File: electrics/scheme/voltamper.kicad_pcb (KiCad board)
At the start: 2 copper layers, 87 x 64 mm, 147 parts, among them K1 swd, K2 servo-1, K3 servo-2, P1 boot, P10 m3-hole, P11 m3-hole, P12 CONN_13X2, P2 boot, P3 -, P4 +, P5 work, P6 aux, P7 ref, P8 m3-hole, P9 m3-hole, Q1 bc857, Q2 bc847, Q3 bc857, Q4 bc847, Q5 irlml2244, Q6 bc847, Q7 bc847, Q8 bc847, SW1 btn-1, SW2 btn-2, U1 CRYSTAL-4PIN, U10 TDA2030A, U11 INA126, U12 SPARTAN-SIP-9007, U2 CP2102, U3 MICRO-USB-B, U4 MCP1703T-3302E/CB, U5 MCP1703T-3302E/CB, U6 NCP3063, U7 SPARTAN-SIP-9007, U8 NCP3063, U9 SPARTAN-SIP-9007

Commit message: Started placig components.
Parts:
- removed C27, C37, C39, C42: 100n, SM0805
- removed C38: 1u, SM0805
- removed D6: lm258a, SO8E
- removed D8: 1N5819, D3
- added C12: 30n, SM0805, F.Cu at (234.0, 167.0)
- added C18: 1n, SM0805, F.Cu at (218.0, 157.0)
- added R56: 16, SM0805, F.Cu at (221.0, 159.0)
- added R57: 16, SM0805, F.Cu at (223.0, 155.0)
- added R58: 410, SM0805, F.Cu at (214.0, 158.0)
- added R59: 410, SM0805, F.Cu at (219.0, 167.0)
- added R60: 0, SM0805, F.Cu at (219.0, 155.0)
- added R61: 16, SM0805, F.Cu at (223.0, 153.0)
- added R62: 16, SM0805, F.Cu at (213.0, 155.0)
- added R67: 10, R4-5, F.Cu at (232.0, 162.0)
- added R70: 16, SM0805, F.Cu at (225.0, 167.0)
- added R71: 16, SM0805, F.Cu at (230.0, 167.0)
- added U13: OPA551, OPA551, F.Cu at (234.0, 146.0)
- added U14: AD825, SO8E, F.Cu at (210.0, 165.0)
- C20, C26, C35: value 100n -> 4u7
- C23, C25, C30: value 10n -> 4u7
- D4: value lm258a -> 1N5819; footprint SO8E -> D3
- R17: value 10k -> 120k
- R18: value 10k -> 10k 0.1%
- R20: value 10 -> 1k
- R25: value 6k8 -> 13.3k 0.1%
- R26: value 1k -> 120k
- R30: value 1k -> 40k 0.1%
- R35: value 1k -> 410
- R39: footprint SM0805 -> SM1206
- U10: value TDA2030A -> ADA4000; footprint TDA2030A -> SOT23-5
- moved D4 57.8 mm to (231.5, 133.0)
- moved C35 57.2 mm to (182.0, 169.0)
- moved R39 55.0 mm to (158.0, 168.0)
- moved C41 46.8 mm to (195.0, 172.0)
- moved U11 46.4 mm to (195.0, 167.5)
- moved R40 46.3 mm to (195.5, 163.5)
- moved Q8 41.6 mm to (167.5, 166.5)
- moved R27 41.3 mm to (163.5, 167.0)
- moved U10 39.4 mm to (183.0, 157.5)
- moved D9 37.6 mm to (163.0, 163.0)
- moved U12 33.1 mm to (178.0, 162.5)
- moved D7 27.1 mm to (234.8, 115.6)
- moved Q6 27.1 mm to (233.8, 122.5)
- moved Q7 27.1 mm to (240.6, 122.4)
- moved R19 27.1 mm to (228.3, 124.6)
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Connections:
- C17 pad 2: GND -> GNDA
- C20 pad 1: N-00000122 -> /f+
- C20 pad 2: GND -> GNDA
- C23 pad 1: GND -> /f-
- C23 pad 2: N-0000091 -> GNDA
- C25 pad 1: N-00000115 -> /v+
- C25 pad 2: N-00000116 -> GNDA
- C26 pad 1: /v+ -> /v-
- C26 pad 2: GND -> GNDA
- C29 pad 2: GND -> GNDA
- C30 pad 1: N-0000023 -> N-0000089
- C30 pad 2: GND -> GNDA
- C33 pad 2: GND -> GNDA
- C34 pad 1: /v+ -> N-0000098
- C34 pad 2: GND -> GNDA
- C35 pad 1: /v+ -> N-0000091
- C35 pad 2: GND -> GNDA
- C40 pad 2: GND -> GNDA
- C41 pad 1: /v- -> N-0000099
- C41 pad 2: GND -> GNDA
- D4 pad 1: /Vpp/2 -> /curr-1
- D4 pad 2: /Vpp/2 -> /v+
- MCU1 pad 12: GND -> GNDA
- P5 pad 1: GND -> GNDA
- Q7 pad 2: N-000009 -> N-0000067
- R17 pad 1: VDD -> N-0000075
- R17 pad 2: N-00000122 -> /eaux-volt
- R18 pad 1: N-00000122 -> VDD
- R18 pad 2: GND -> N-0000090
- R20 pad 2: N-0000091 -> N-0000077
- R21 pad 2: N-0000091 -> N-0000077
- R22 pad 1: /Vpp/2 -> /curr-en
- R22 pad 2: N-00000115 -> N-0000067
- R25 pad 1: N-00000116 -> GNDA
- R25 pad 2: N-00000115 -> N-0000090
- R26 pad 1: /curr-en -> N-0000066
- R26 pad 2: N-000009 -> GNDA
- R30 pad 1: N-0000023 -> N-0000092
- R30 pad 2: N-00000116 -> N-0000090
- R32 pad 2: GND -> GNDA
- R33 pad 2: /Eaux-test -> /eaux-volt
- R35 pad 1: N-0000029 (its old number) -> /Iref
- R35 pad 2: /Eref-test -> N-0000068
- R37 pad 2: GND -> GNDA
- R38 pad 2: /Eref-test -> /eref-volt
- R39 pad 1: N-00000119 (its old number) -> N-0000070
- R39 pad 2: /Eaux -> /eaux-volt
- R42 pad 2: GND -> GNDA
- U10 pad 1: N-0000023 -> N-0000092
- U10 pad 2: N-0000095 (its old number) -> N-0000090
- U10 pad 3: /v- -> N-0000077
- U10 pad 4: N-00000119 (its old number) -> /f-
- U10 pad 5: /v+ -> (no net)
- U11 pad 2: /Eaux -> N-0000070
- U11 pad 3: N-00000119 (its old number) -> /eaux-volt
- U11 pad 4: /v- -> N-0000099
- U11 pad 5: GND -> GNDA
- U11 pad 7: /v+ -> N-0000098
- U12 pad 1: /Eaux -> N-0000070
- U5 pad 1: GND -> GNDA
- U7 pad 1: N-0000095 (its old number) -> N-0000075
- U7 pad 3: /volt-1 -> /curr-1
- U7 pad 4: N-0000029 (its old number) -> N-0000068
- U9 pad 1: N-0000095 (its old number) -> N-0000075
- U9 pad 3: /curr-1 -> /volt-1
- U9 pad 4: /Iref -> N-0000069
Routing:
- net GND: track 632.0 -> 447.9 mm, vias 4 -> 2
- net /v+: track 201.3 -> 22.7 mm, vias 1 -> 0
- net /v-: track 109.7 -> 55.4 mm
- net /Iref: track 53.1 -> 0.00 mm, vias 1 -> 0
- net /curr-en: track 52.4 -> 0.00 mm, vias 3 -> 0
- net /volt-en: track 46.5 -> 0.00 mm, vias 3 -> 0
- net /Eref-test: track 44.9 -> 0.00 mm, vias 1 -> 0
- net /Eaux-test: track 34.8 -> 0.00 mm, vias 1 -> 0
- net GNDA: track 0.00 -> 32.6 mm
- net N-0000095 (its old number): track 24.2 -> 0.00 mm
- net /Eaux: track 21.0 -> 0.00 mm, vias 1 -> 0
- net /aux-en: track 18.5 -> 0.00 mm, vias 1 -> 0
- net N-0000034: track 17.7 -> 0.00 mm
- net N-00000116: track 17.0 -> 0.00 mm, vias 1 -> 0
- net N-00000115: track 16.0 -> 0.00 mm
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- removed copper zone on B.Cu, net GND
- removed copper zone on F.Cu, net GND
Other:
- outline, holes or cut-outs redrawn

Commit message: a
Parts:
- added D6: 1N5819, D3, F.Cu at (193.8, 139.5)
- added Q9: bc847, SOT23EBC, F.Cu at (217.1, 154.1)
- added R63: 1k, SM0805, F.Cu at (217.1, 154.1)
- added U15: SPARTAN-SIP-9007, SPARTAN-SIP-9007, F.Cu at (194.0, 143.7)
- C25, C26, C34, C41, D4, D9, R17, R35, R40, U11: moved to F.Cu
- moved R71 73.9 mm to (158.4, 148.7)
- moved R67 71.0 mm to (161.8, 151.4), turned to 180 degrees
- moved R41 66.2 mm to (235.5, 103.0)
- moved R70 63.6 mm to (166.4, 142.2), turned to 270 degrees
- moved R35 57.3 mm to (175.6, 139.6), turned to 0 degrees
- moved C12 50.6 mm to (195.3, 134.3), turned to 270 degrees
- moved C23 49.7 mm to (223.0, 99.5)
- moved R18 49.5 mm to (227.0, 100.0)
- moved R42 49.4 mm to (221.5, 107.0)
- moved C40 49.3 mm to (219.5, 106.5)
- moved C20 48.6 mm to (225.5, 104.5)
- moved R43 46.1 mm to (219.0, 110.0)
- moved R36 45.3 mm to (220.0, 103.5)
- moved C33 44.9 mm to (223.5, 112.5)
- moved R38 44.2 mm to (222.5, 110.0)
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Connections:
- net N-0000070 renamed /aux-pre
- C18 pad 1: N-0000090 -> N-0000088
- C5 pad 2: GND -> GNDA
- MCU1 pad 52: (no net) -> /short-en
- R18 pad 2: N-0000090 -> N-0000088
- R25 pad 2: N-0000090 -> N-0000088
- R30 pad 2: N-0000090 -> N-0000088
- U10 pad 2: N-0000090 -> /f-
- U10 pad 4: /f- -> N-0000088
- U10 pad 5: (no net) -> /f+
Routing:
- net /v-: track 55.4 -> 28.8 mm
- net /AVdd: track 34.3 -> 9.08 mm
- net GNDA: track 32.6 -> 8.87 mm
- net /Eaux-in: track 29.4 -> 12.7 mm
- net /Eref-in: track 24.1 -> 12.5 mm
- net /Iref-in: track 18.7 -> 11.6 mm
- net /eaux-volt: track 2.81 -> 0.00 mm
- net /v+: track 22.7 -> 20.6 mm
- net /f+: track 1.85 -> 0.00 mm
- net /f-: track 1.64 -> 0.00 mm
- net (no net): track 1.27 -> 0.00 mm
- net GND: track 447.9 -> 446.7 mm
- net N-0000090: track 0.80 -> 0.00 mm

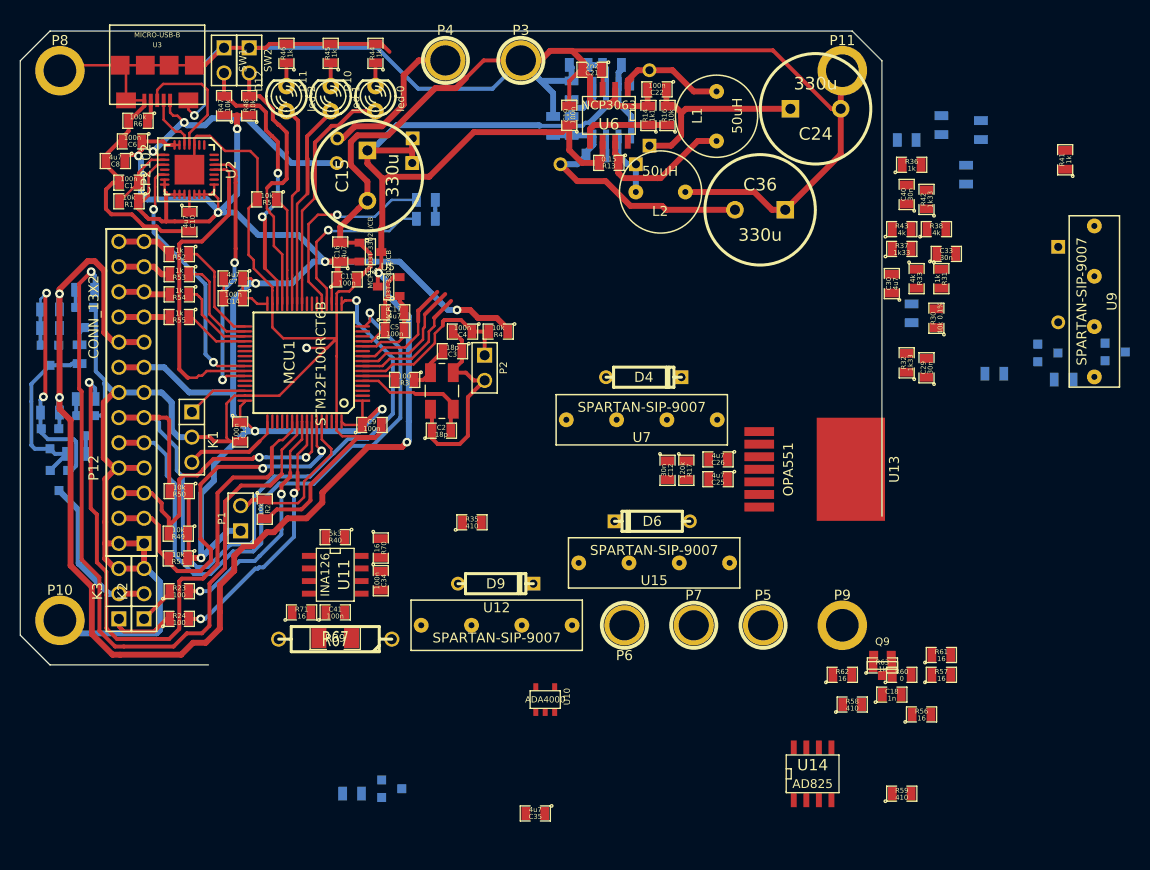
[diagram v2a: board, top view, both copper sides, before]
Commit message: Placing elements. Finally decided to make software current feedback.
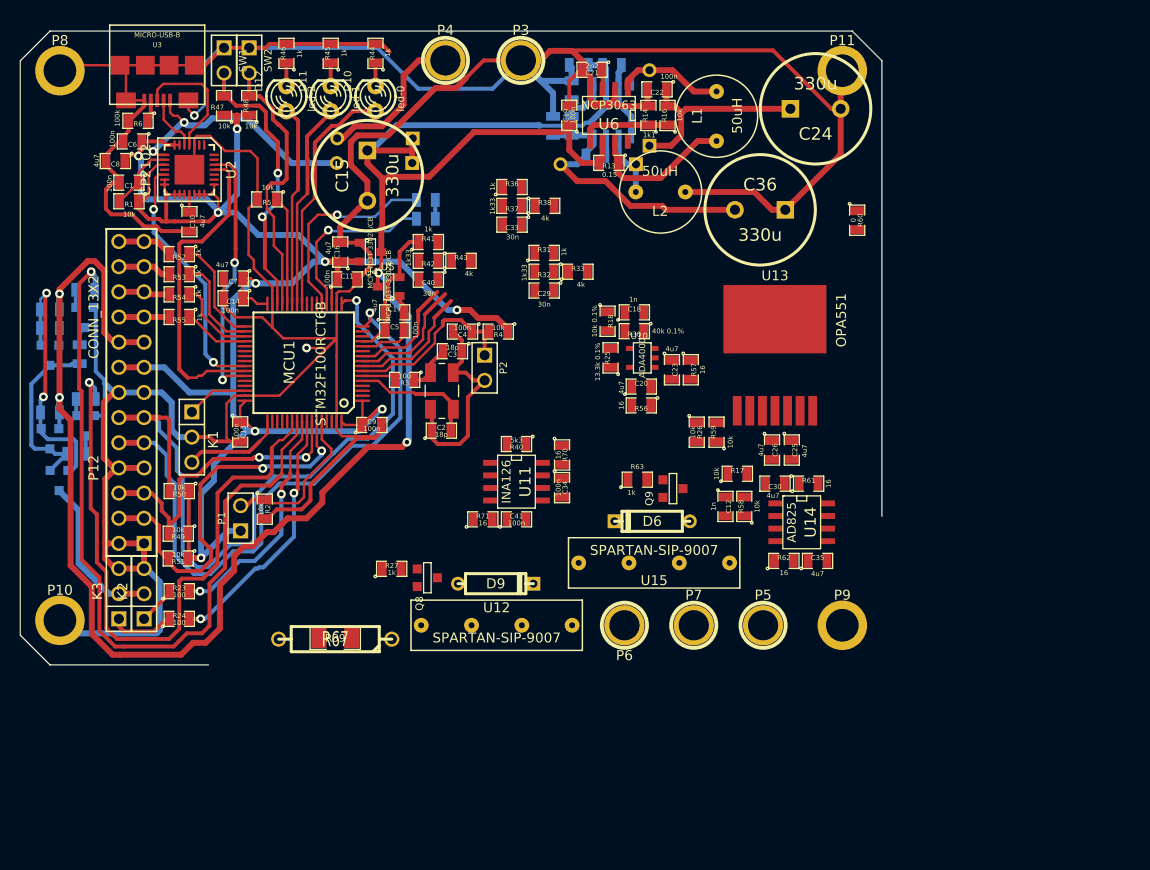
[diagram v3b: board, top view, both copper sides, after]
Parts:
- removed D4, D7: 1N5819, D3
- removed Q6, Q7: bc847, SOT23EBC
- removed R19, R22: 1k, SM0805
- removed R35: 410, SM0805
- removed U7, U9: SPARTAN-SIP-9007, SPARTAN-SIP-9007
- C12: value 30n -> 1n
- C20, C23, Q8, R18, R25, R27: moved to F.Cu
- R17: value 120k -> 10k
- R26: value 120k -> 10k; moved to F.Cu
- R58, R59: value 410 -> 10k
- moved R41 64.8 mm to (171.2, 111.3), turned to 0 degrees
- moved R42 50.7 mm to (171.2, 113.2), turned to 180 degrees
- moved C40 49.1 mm to (171.2, 115.1), turned to 180 degrees
- moved C18 46.5 mm to (192.0, 118.4)
- moved R60 46.1 mm to (214.5, 109.1), turned to 270 degrees
- moved R43 44.6 mm to (174.5, 113.2)
- moved C33 43.9 mm to (179.7, 109.5), turned to 180 degrees
- moved R18 42.4 mm to (189.3, 119.3)
- moved R56 42.1 mm to (192.7, 127.8), turned to 180 degrees
- moved R59 41.0 mm to (200.3, 130.5), turned to 90 degrees
- moved R36 40.4 mm to (179.7, 105.8)
- moved R31 40.2 mm to (182.9, 112.4), turned to 0 degrees
- moved R57 39.9 mm to (197.7, 124.2), turned to 270 degrees
- moved R38 39.6 mm to (182.9, 107.7)
- moved R37 39.6 mm to (179.7, 107.7), turned to 180 degrees
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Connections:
- C12 pad 1: N-0000078 (its old number) -> N-0000071
- C12 pad 2: /eaux-volt -> /eref-volt
- MCU1 pad 2: /volt-en -> (no net)
- MCU1 pad 52: /short-en -> (no net)
- MCU1 pad 61: /curr-en -> /short-en
- R17 pad 1: N-0000078 (its old number) -> N-0000071
- R17 pad 2: /eaux-volt -> GNDA
- R18 pad 1: VDD -> /AVdd
- R58 pad 2: N-0000063 -> N-0000071
- U13 pad 2: N-0000078 (its old number) -> N-0000071
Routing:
- net GND: track 446.7 -> 453.2 mm
- net /AVdd: track 9.08 -> 14.0 mm

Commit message: a
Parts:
- moved R39 20.1 mm to (180.1, 142.9)
- moved R67 18.4 mm to (178.2, 142.9)
- moved R71 10.7 mm to (184.7, 132.2), turned to 180 degrees
- moved R70 10.0 mm to (176.6, 138.7), turned to 90 degrees
- moved R40 8.20 mm to (181.2, 139.8), turned to 0 degrees
- moved C34 8.13 mm to (176.6, 135.4), turned to 90 degrees
- moved C41 7.18 mm to (181.2, 132.2), turned to 180 degrees
- moved R62 3.65 mm to (210.8, 143.5)
- moved C35 3.15 mm to (207.3, 143.5), turned to 180 degrees
- moved C29 2.78 mm to (180.2, 115.8)
- moved R32 2.78 mm to (180.2, 113.9)
- moved R33 2.78 mm to (183.6, 113.9)
- moved R59 2.58 mm to (198.4, 128.8), turned to 270 degrees
- moved R26 2.06 mm to (200.3, 130.7)
- moved D9 1.75 mm to (179.8, 145.8)
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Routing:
- net GNDA: track 8.87 -> 149.2 mm, vias 0 -> 3
- net /v-: track 28.8 -> 145.7 mm, vias 0 -> 4
- net /eaux-volt: track 0.00 -> 88.7 mm, vias 0 -> 2
- net GND: track 453.2 -> 527.4 mm
- net /eref-volt: track 0.00 -> 67.9 mm
- net /short-en: track 0.00 -> 34.9 mm, vias 0 -> 2
- net /AVdd: track 14.0 -> 47.8 mm
- net N-0000075: track 1.90 -> 35.4 mm, vias 0 -> 1
- net /Iref: track 0.00 -> 32.4 mm, vias 0 -> 2
- net /aux-pre: track 0.00 -> 31.5 mm
- net /v+: track 20.6 -> 49.5 mm
- net /aux-en: track 0.00 -> 18.8 mm, vias 0 -> 2
- net /Eref-in: track 12.5 -> 30.5 mm
- net /Eaux-in: track 12.7 -> 29.9 mm
- net N-0000078: track 0.00 -> 15.6 mm
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
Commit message: Prepared gerbers. Needs extensions and file names adjustment.
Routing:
- net /v+: track 49.5 -> 205.7 mm, vias 0 -> 3
- net GNDA: track 149.2 -> 254.6 mm, vias 3 -> 6
- net GND: track 527.4 -> 596.3 mm
- net /eaux-volt: track 88.7 -> 87.8 mm
- added copper zone on B.Cu, net GND
- added copper zone on F.Cu, net GND
- added copper zone on B.Cu, net GNDA
- added copper zone on F.Cu, net GNDA
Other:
- outline, holes or cut-outs redrawn
